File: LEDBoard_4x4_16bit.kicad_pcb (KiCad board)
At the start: 2 copper layers, 39.5 x 39.5 mm, 35 parts, among them J1 signal_in, J2 power, J6 signal_out, U1 TLC5971RGER, U2 TLC5971RGER, U3 TLC5971RGER, U4 TLC5971RGER

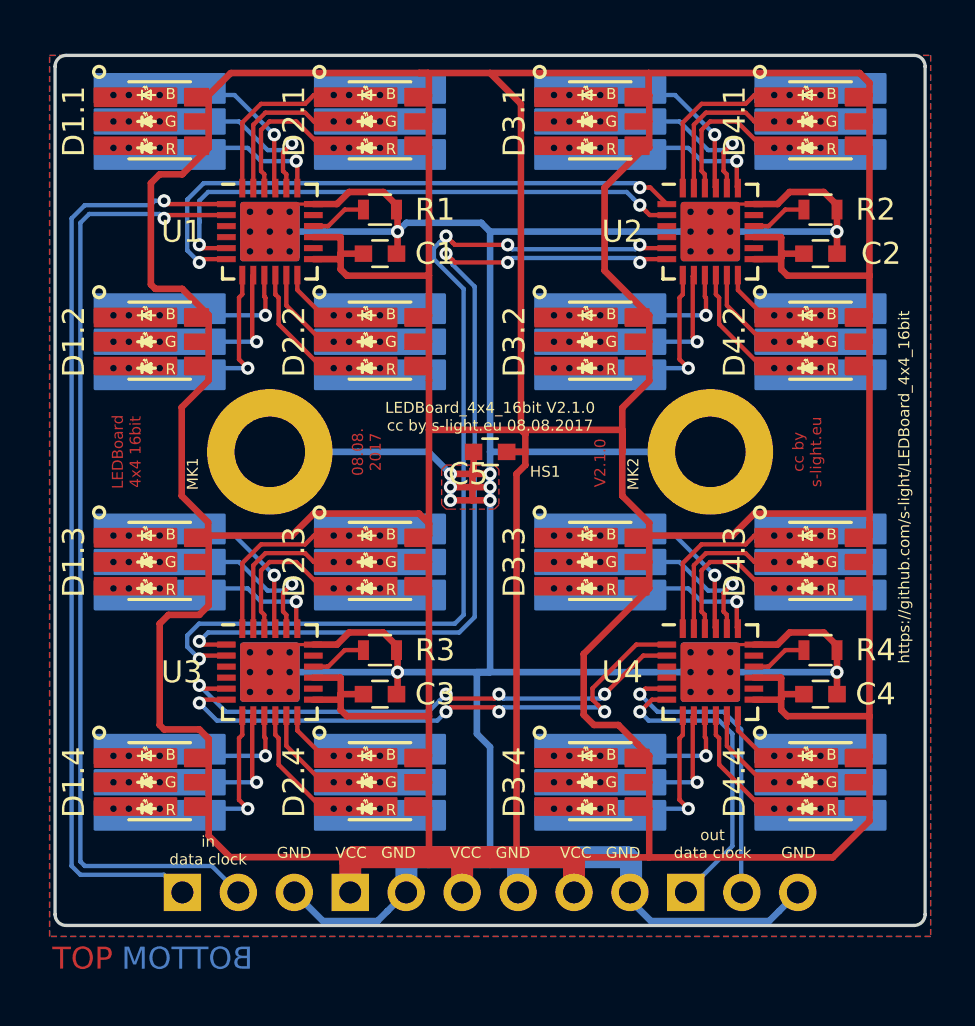
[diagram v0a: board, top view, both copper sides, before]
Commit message: started to do variant with TLC5971PWP --> HTSSOP housing
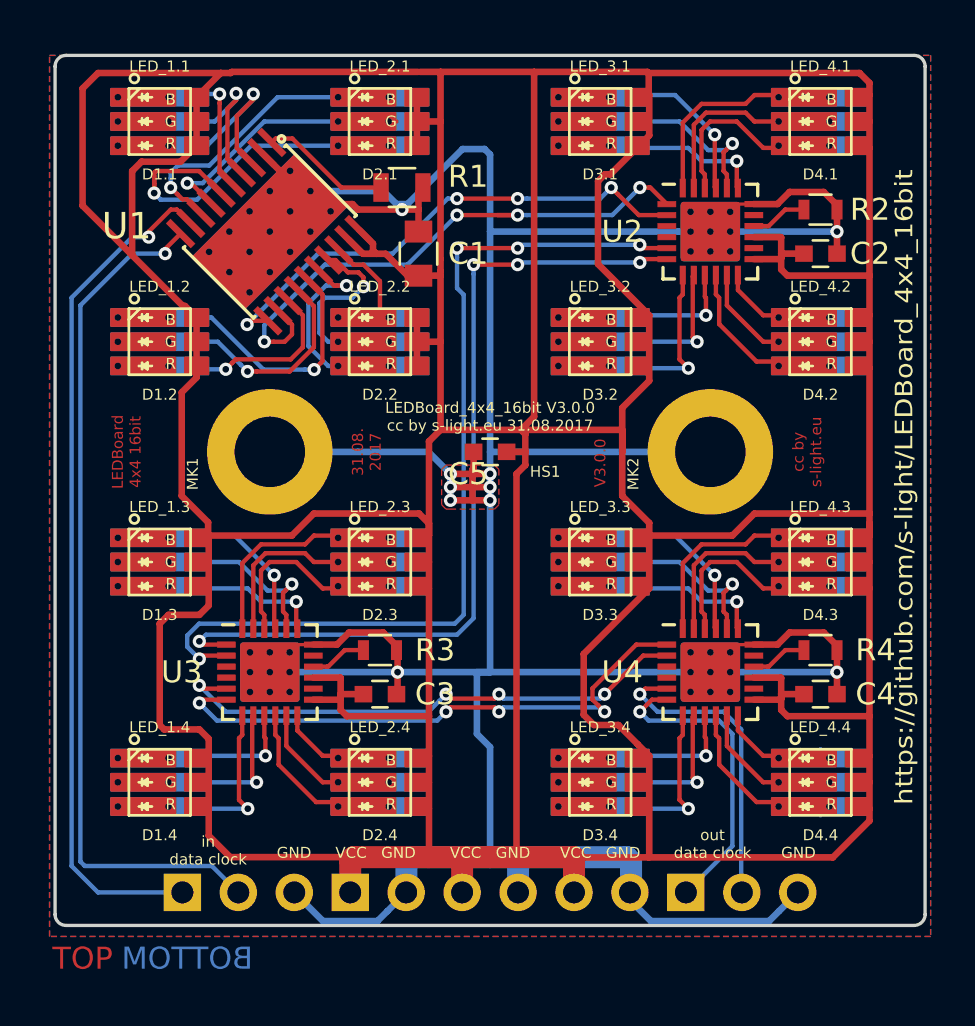
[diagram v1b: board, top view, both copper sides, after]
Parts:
- C1: footprint Capacitors_SMD:C_0603 -> Capacitors_SMD:C_0805
- D1.1, D1.2, D1.3, D1.4, D2.1, D2.2, D2.3, D2.4, D3.1, D3.2, D3.3, D3.4, D4.1, D4.2, D4.3, D4.4: footprint nichia:LED_NSSM124_wViaHeatSinkBig_LayoutCompatibleWithNSSM032AT -> nichia:LED_NSSM124_wViaHeatSinkBig
- R1: footprint Resistors_SMD:R_0603 -> Resistors_SMD:R_0805
- U1: value TLC5971RGER -> TLC5971PWPR; footprint Housings_DFN_QFN:Texas_S-PVQFN-N24_ThermalVias -> Housings_SSOP:HTSSOP-20-1EP_4.4x6.5mm_Pitch0.65mm_ThermalVias_TI_R-PDSO-G20
- moved C1 1.75 mm to (66.8, 59.0), turned to 90 degrees
- moved R1 1.41 mm to (66.0, 56.0)
- turned U1 to 315 degrees
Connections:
- U1 pad 1: /data_in -> /U1_sense
- U1 pad 10: /LED_2.2_R -> /clock_in
- U1 pad 11: /LED_2.2_G -> /clock_0-1
- U1 pad 12: /LED_2.2_B -> /data_0-1
- U1 pad 13: VCC -> /LED_1.2_R
- U1 pad 14: Net-(U1-Pad14) -> /LED_1.2_G
- U1 pad 15: VCC -> /LED_1.2_B
- U1 pad 16: /U1_sense -> /LED_2.2_R
- U1 pad 17: (no net) -> /LED_2.2_G
- U1 pad 18: GND -> /LED_2.2_B
- U1 pad 19: /LED_1.1_R -> VCC
- U1 pad 2: /clock_in -> GND
- U1 pad 20: /LED_1.1_G -> VCC
- U1 pad 21: /LED_1.1_B -> GND
- U1 pad 3: Net-(U1-Pad3) -> /LED_1.1_R
- U1 pad 4: Net-(U1-Pad4) -> /LED_1.1_G
- U1 pad 5: /clock_0-1 -> /LED_1.1_B
- U1 pad 6: /data_0-1 -> /LED_2.1_R
- U1 pad 7: /LED_1.2_R -> /LED_2.1_G
- U1 pad 8: /LED_1.2_G -> /LED_2.1_B
- U1 pad 9: /LED_1.2_B -> /data_in
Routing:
- net VCC: track 326.2 -> 344.5 mm
- net /LED_2.1_R: track 7.76 -> 16.6 mm, vias 0 -> 1
- net /LED_1.2_B: track 6.65 -> 12.5 mm
- net /LED_2.1_G: track 8.02 -> 12.9 mm, vias 0 -> 1
- net GND: track 176.0 -> 180.7 mm
- net /LED_2.1_B: track 8.74 -> 13.4 mm, vias 0 -> 1
- net /clock_in: track 43.7 -> 39.0 mm
- net /data_in: track 42.3 -> 38.8 mm
- net /LED_1.2_G: track 7.53 -> 10.9 mm
- net /U1_sense: track 2.59 -> 5.91 mm
- net /LED_2.2_G: track 5.61 -> 8.91 mm, vias 0 -> 1
- net /LED_1.1_R: track 7.69 -> 11.0 mm
- net /data_1-2: track 41.7 -> 39.1 mm
- net /LED_2.2_R: track 7.02 -> 9.20 mm, vias 0 -> 1
- net /clock_0-1: track 25.2 -> 23.2 mm, vias 2 -> 4
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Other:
- net class Default: clearance 0 -> 0.15
- rule trace_clearance: 0 -> 0.15
- board text added: "31.08. 2017"
- board text added: "LEDBoard_4x4_16bit V3.0.0 cc by s-light.eu 31.08.2017"
- board text added: "V3.0.0"
- board text removed: "08.08. 2017"
- board text removed: "LEDBoard_4x4_16bit V2.1.0 cc by s-light.eu 08.08.2017"
- board text removed: "V2.1.0"

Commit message: preparation for new housings
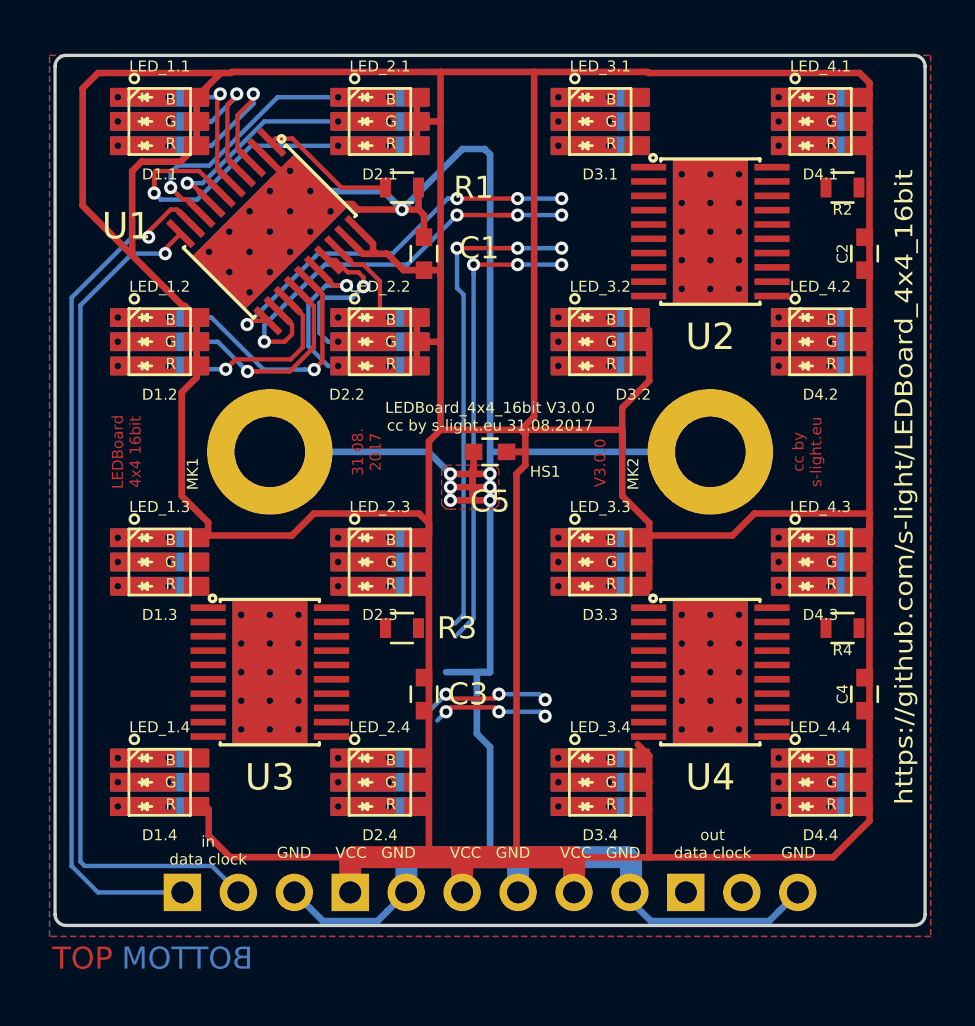
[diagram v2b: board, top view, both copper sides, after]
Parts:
- C1: footprint Capacitors_SMD:C_0805 -> Capacitors_SMD:C_0603
- R1: footprint Resistors_SMD:R_0805 -> Resistors_SMD:R_0603
- U2, U3, U4: value TLC5971RGER -> TLC5971PWPR; footprint Housings_DFN_QFN:Texas_S-PVQFN-N24_ThermalVias -> Housings_SSOP:HTSSOP-20-1EP_4.4x6.5mm_Pitch0.65mm_ThermalVias_TI_R-PDSO-G20
- moved C2 2.00 mm to (87.0, 59.0), turned to 90 degrees
- moved C3 2.00 mm to (67.0, 79.0), turned to 90 degrees
- moved C4 2.00 mm to (87.0, 79.0), turned to 90 degrees
- moved R2 1.41 mm to (86.0, 56.0)
- moved R3 1.41 mm to (66.0, 76.0)
- moved R4 1.41 mm to (86.0, 76.0)
- moved C1 0.25 mm to (67.0, 59.0)
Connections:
- U2 pad 1: /data_0-1 -> /U2_sense
- U2 pad 10: /LED_4.2_R -> /clock_0-1
- U2 pad 11: /LED_4.2_G -> /clock_1-2
- U2 pad 12: /LED_4.2_B -> /data_1-2
- U2 pad 13: VCC -> /LED_3.2_R
- U2 pad 14: Net-(U2-Pad14) -> /LED_3.2_G
- U2 pad 15: VCC -> /LED_3.2_B
- U2 pad 16: /U2_sense -> /LED_4.2_R
- U2 pad 17: (no net) -> /LED_4.2_G
- U2 pad 18: GND -> /LED_4.2_B
- U2 pad 19: /LED_3.1_R -> VCC
- U2 pad 2: /clock_0-1 -> GND
- U2 pad 20: /LED_3.1_G -> VCC
- U2 pad 21: /LED_3.1_B -> GND
- U2 pad 3: Net-(U2-Pad3) -> /LED_3.1_R
- U2 pad 4: Net-(U2-Pad4) -> /LED_3.1_G
- U2 pad 5: /clock_1-2 -> /LED_3.1_B
- U2 pad 6: /data_1-2 -> /LED_4.1_R
- U2 pad 7: /LED_3.2_R -> /LED_4.1_G
- U2 pad 8: /LED_3.2_G -> /LED_4.1_B
- U2 pad 9: /LED_3.2_B -> /data_0-1
- U3 pad 1: /data_1-2 -> /U3_sense
- U3 pad 10: /LED_2.4_R -> /clock_1-2
- U3 pad 11: /LED_2.4_G -> /clock_2-3
- U3 pad 12: /LED_2.4_B -> /data_2-3
- U3 pad 13: VCC -> /LED_1.4_R
- U3 pad 14: Net-(U3-Pad14) -> /LED_1.4_G
- U3 pad 15: VCC -> /LED_1.4_B
- U3 pad 16: /U3_sense -> /LED_2.4_R
- U3 pad 17: (no net) -> /LED_2.4_G
- U3 pad 18: GND -> /LED_2.4_B
- U3 pad 19: /LED_1.3_R -> VCC
- U3 pad 2: /clock_1-2 -> GND
- U3 pad 20: /LED_1.3_G -> VCC
- U3 pad 21: /LED_1.3_B -> GND
- U3 pad 3: Net-(U3-Pad3) -> /LED_1.3_R
- U3 pad 4: Net-(U3-Pad4) -> /LED_1.3_G
- U3 pad 5: /clock_2-3 -> /LED_1.3_B
- U3 pad 6: /data_2-3 -> /LED_2.3_R
- U3 pad 7: /LED_1.4_R -> /LED_2.3_G
- U3 pad 8: /LED_1.4_G -> /LED_2.3_B
- U3 pad 9: /LED_1.4_B -> /data_1-2
- U4 pad 1: /data_2-3 -> /U4_sense
- U4 pad 10: /LED_4.4_R -> /clock_2-3
- U4 pad 11: /LED_4.4_G -> /clock_out
- U4 pad 12: /LED_4.4_B -> /data_out
- U4 pad 13: VCC -> /LED_3.4_R
- U4 pad 14: Net-(U4-Pad14) -> /LED_3.4_G
- U4 pad 15: VCC -> /LED_3.4_B
- U4 pad 16: /U4_sense -> /LED_4.4_R
- U4 pad 17: (no net) -> /LED_4.4_G
- U4 pad 18: GND -> /LED_4.4_B
- U4 pad 19: /LED_3.3_R -> VCC
- U4 pad 2: /clock_2-3 -> GND
- U4 pad 20: /LED_3.3_G -> VCC
- U4 pad 21: /LED_3.3_B -> GND
- U4 pad 3: Net-(U4-Pad3) -> /LED_3.3_R
- U4 pad 4: Net-(U4-Pad4) -> /LED_3.3_G
- U4 pad 5: /clock_out -> /LED_3.3_B
- U4 pad 6: /data_out -> /LED_4.3_R
- U4 pad 7: /LED_3.4_R -> /LED_4.3_G
- U4 pad 8: /LED_3.4_G -> /LED_4.3_B
- U4 pad 9: /LED_3.4_B -> /data_2-3
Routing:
- net GND: track 180.7 -> 112.5 mm, vias 10 -> 7
- net VCC: track 344.5 -> 277.3 mm
- net /data_2-3: track 26.0 -> 5.31 mm, vias 4 -> 3
- net /clock_1-2: track 41.9 -> 22.1 mm, vias 4 -> 3
- net /clock_2-3: track 24.4 -> 5.90 mm, vias 4 -> 3
- net /data_1-2: track 39.1 -> 21.1 mm, vias 4 -> 3
- net /data_out: track 14.1 -> 0.00 mm, vias 1 -> 0
- net /clock_out: track 14.0 -> 0.00 mm, vias 1 -> 0
- net /LED_4.4_R: track 10.1 -> 0.00 mm
- net /LED_3.3_G: track 8.92 -> 0.00 mm, vias 1 -> 0
- net /LED_3.1_G: track 8.92 -> 0.00 mm, vias 1 -> 0
- net /LED_1.3_G: track 8.92 -> 0.00 mm, vias 1 -> 0
- net /LED_4.3_B: track 8.74 -> 0.00 mm
- net /LED_2.3_B: track 8.74 -> 0.00 mm
- net /LED_4.1_B: track 8.74 -> 0.00 mm
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
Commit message: updated driver housings + reroute
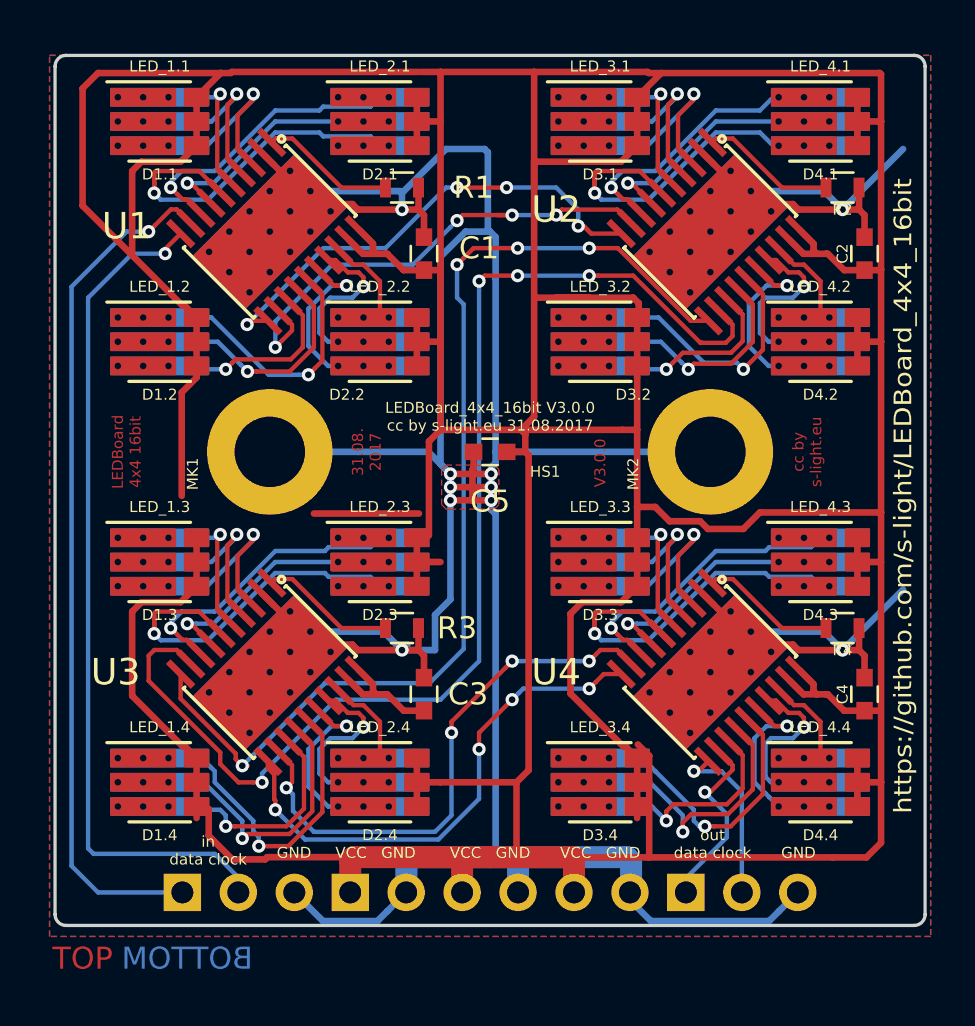
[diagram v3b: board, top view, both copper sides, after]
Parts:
- turned U2 to 315 degrees
- turned U3 to 315 degrees
- turned U4 to 315 degrees
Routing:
- net GND: track 112.5 -> 185.5 mm, vias 7 -> 10
- net VCC: track 277.3 -> 344.0 mm
- net /data_1-2: track 21.1 -> 54.9 mm, vias 3 -> 4
- net /clock_1-2: track 22.1 -> 48.5 mm, vias 3 -> 4
- net /data_2-3: track 5.31 -> 25.1 mm, vias 3 -> 4
- net /clock_2-3: track 5.90 -> 23.5 mm, vias 3 -> 4
- net /LED_2.3_R: track 0.00 -> 17.1 mm, vias 0 -> 1
- net /LED_4.3_R: track 0.00 -> 17.1 mm, vias 0 -> 1
- net /LED_4.1_R: track 0.00 -> 17.1 mm, vias 0 -> 1
- net /LED_1.4_B: track 0.00 -> 14.9 mm, vias 0 -> 1
- net /LED_4.3_B: track 0.00 -> 13.2 mm, vias 0 -> 1
- net /LED_2.3_B: track 0.00 -> 13.2 mm, vias 0 -> 1
- net /LED_4.1_B: track 0.00 -> 13.2 mm, vias 0 -> 1
- net /LED_3.4_B: track 0.00 -> 13.2 mm, vias 0 -> 1
- net /LED_1.4_G: track 0.00 -> 12.9 mm, vias 0 -> 1
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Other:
- net class Default: clearance 0.15 -> 0
- rule trace_clearance: 0.15 -> 0

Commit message: updated exports and images
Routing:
- net /data_1-2: track 54.9 -> 54.4 mm

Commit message: pcb: temporary remove layer-alignment-target
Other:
- net class Default: trace_width 0.2 -> 0.25
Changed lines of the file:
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@@
-(kicad_pcb (version 20170123) (host pcbnew no-vcs-found-3ac87f6~59~ubuntu17.04.1)
+(kicad_pcb (version 20170123) (host pcbnew no-vcs-found-1fe91e6~59~ubuntu17.04.1)
   (general
     (thickness 1.6)
-    (drawings 52)
+    (drawings 51)
     (tracks 1025)
     (zones 0)
@@
   )
   (setup
-    (last_trace_width 0.2)
+    (last_trace_width 0.25)
     (user_trace_width 0.15)
     (user_trace_width 0.2)
@@
   (net_class Default "This is the default net class."
     (clearance 0)
-    (trace_width 0.2)
+    (trace_width 0.25)
     (via_dia 0.6)
     (via_drill 0.3)
@@
     )
   )
-  (target plus (at 50 50) (size 5) (width 0.15) (layer Edge.Cuts))
   (gr_line (start 88 86) (end 52 86) (layer B.SilkS) (width 0.2))
   (gr_line (start 88 50) (end 88 86) (layer B.SilkS) (width 0.2))

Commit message: updated smd pads to roundedrect version
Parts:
- D1.1, D1.2, D1.3, D1.4, D2.1, D2.2, D2.3, D2.4, D3.1, D3.2, D3.3, D3.4, D4.1, D4.2, D4.3, D4.4: footprint nichia:LED_NSSM124_wViaHeatSinkBig -> nichia:LED_NSSM124_wViaHeatSinkBig_roundedPads
- U1, U2, U3, U4: footprint Housings_SSOP:HTSSOP-20-1EP_4.4x6.5mm_Pitch0.65mm_ThermalVias_TI_R-PDSO-G20 -> Housings_SSOP:HTSSOP-20-1EP_4.4x6.5mm_Pitch0.65mm_ThermalVias_TI_R-PDSO-G20_roundedPads
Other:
- board text added: "27.09. 2017"
- board text added: "LEDBoard_4x4_16bit V3.0.1 cc by s-light.eu 27.09.2017"
- board text added: "V3.0.1"
- board text removed: "31.08. 2017"
- board text removed: "LEDBoard_4x4_16bit V3.0.0 cc by s-light.eu 31.08.2017"
- board text removed: "V3.0.0"

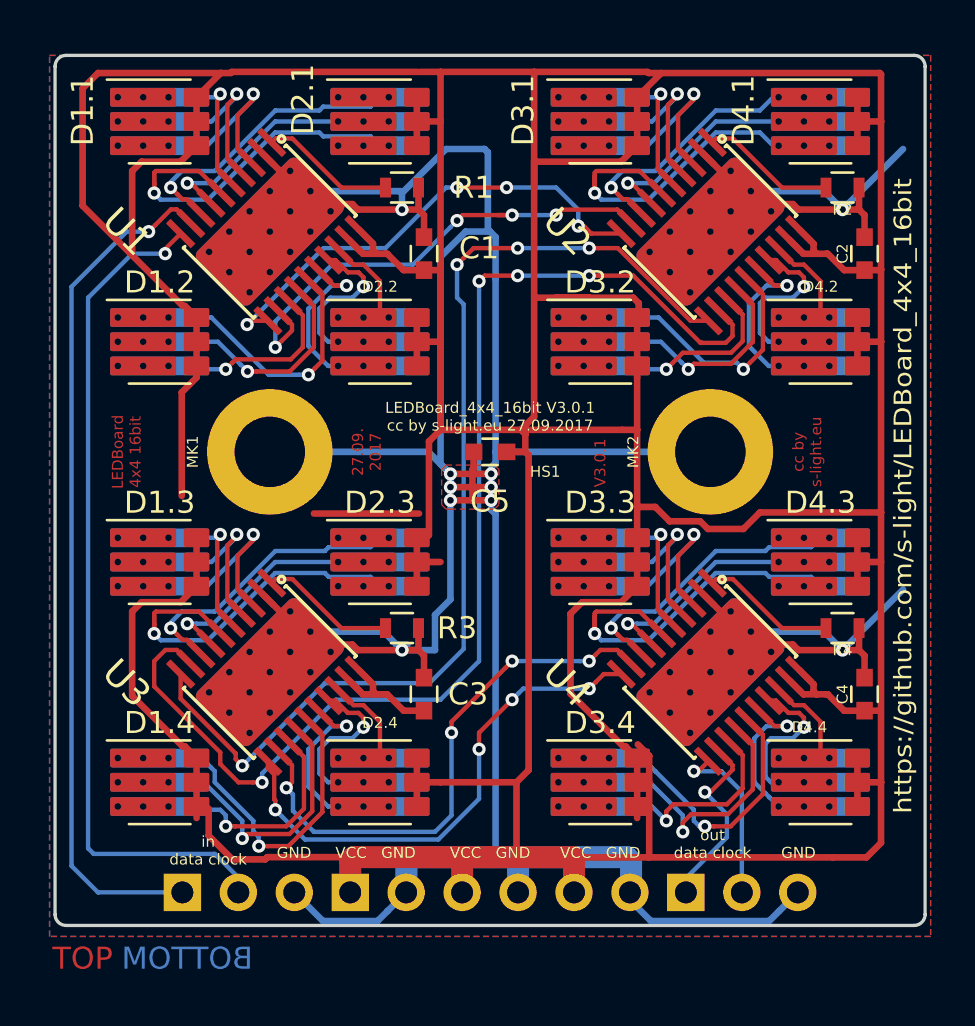
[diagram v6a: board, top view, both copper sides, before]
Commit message: updated Resistors and Capacitors for easier handsoldering
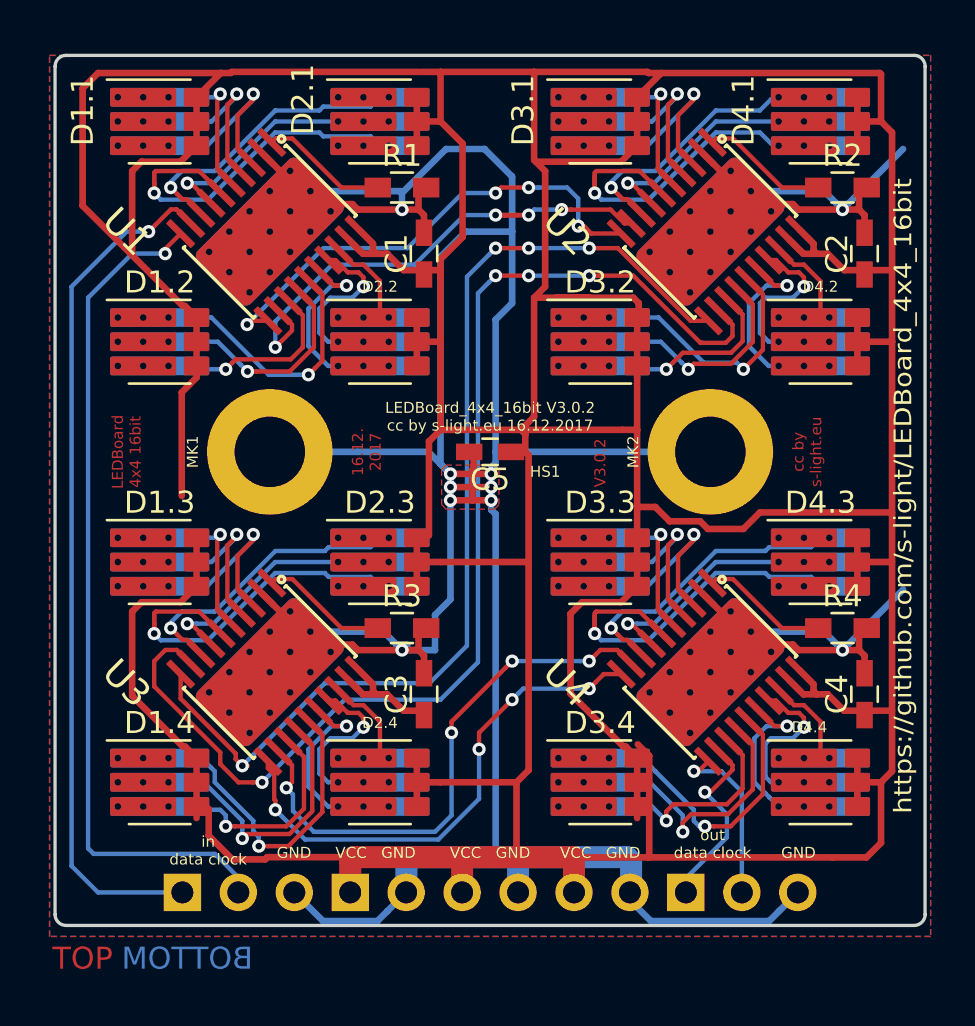
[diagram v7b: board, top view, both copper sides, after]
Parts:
- C1, C2, C3, C4, C5: footprint Capacitors_SMD:C_0603 -> Capacitors_SMD:C_0603_HandSoldering
- R1, R2, R3, R4: footprint Resistors_SMD:R_0603 -> Resistors_SMD:R_0603_HandSoldering
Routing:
- net VCC: track 344.0 -> 346.2 mm
- net /data_0-1: track 22.6 -> 24.4 mm
- net GND: track 185.5 -> 187.1 mm
- net /clock_1-2: track 48.5 -> 47.6 mm
- net /data_1-2: track 54.4 -> 53.9 mm
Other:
- board text added: "16.12. 2017"
- board text added: "LEDBoard_4x4_16bit V3.0.2 cc by s-light.eu 16.12.2017"
- board text added: "V3.0.2"
- board text removed: "27.09. 2017"
- board text removed: "LEDBoard_4x4_16bit V3.0.1 cc by s-light.eu 27.09.2017"
- board text removed: "V3.0.1"
